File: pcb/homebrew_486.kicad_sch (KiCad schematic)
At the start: 4 parts

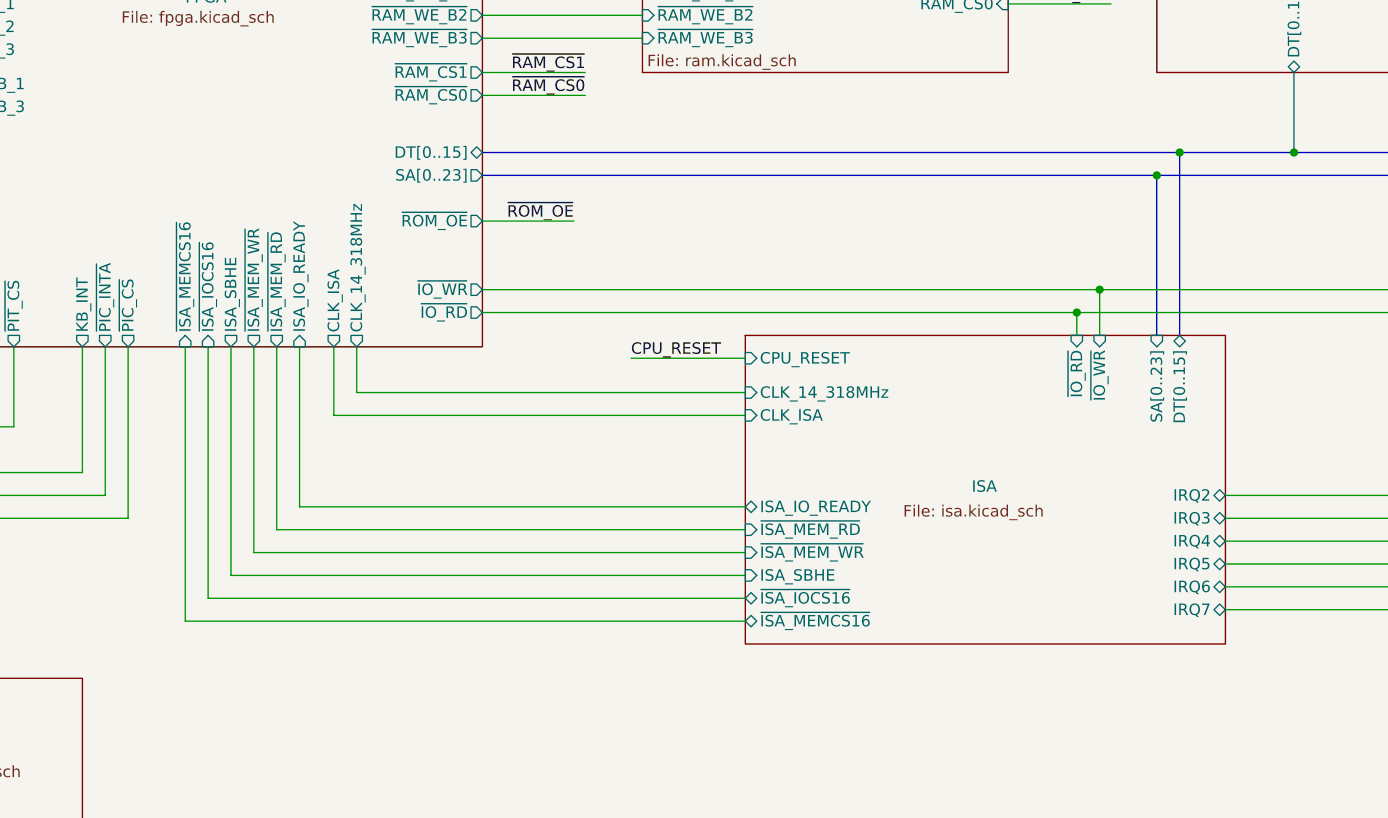
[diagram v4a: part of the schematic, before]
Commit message: handle ISA_BALE by FPGA
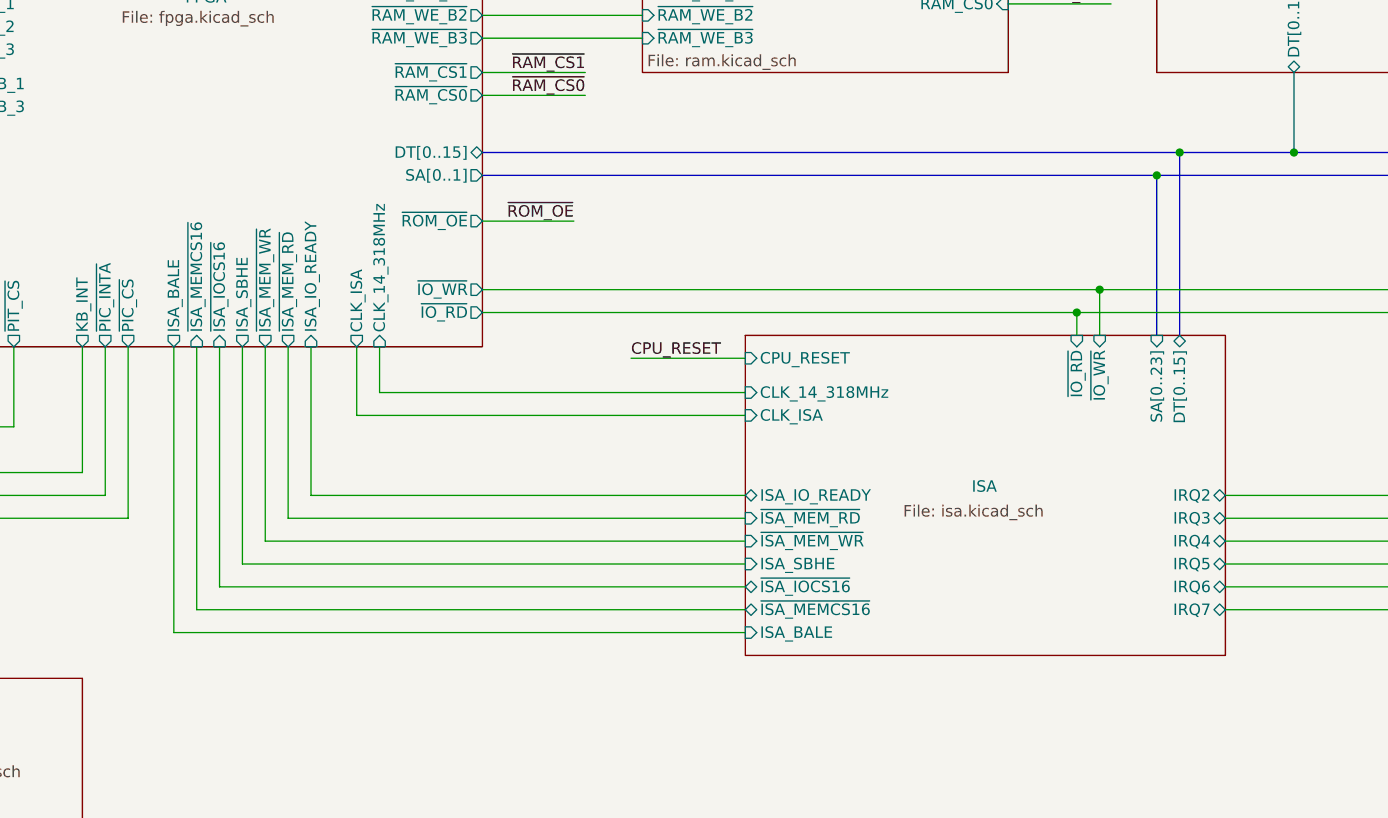
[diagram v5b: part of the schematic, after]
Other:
- sheet FPGA ports: added ISA_BALE, SA[0..1]; removed SA[0..23]
- sheet ISA ports: added ISA_BALE; removed none
